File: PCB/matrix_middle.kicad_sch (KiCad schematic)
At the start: 62 parts, among them J10 Conn_02x04_Top_Bottom, J11 Conn_01x04, J12 Conn_02x04_Top_Bottom, J13 Conn_01x04, J14 Conn_02x04_Top_Bottom, J15 Conn_02x02_Top_Bottom, J17 Conn_02x02_Top_Bottom, J19 Conn_02x02_Top_Bottom, J20 Conn_02x02_Top_Bottom, J25 Conn_01x04, J27 Conn_01x04, J9 Conn_02x04_Top_Bottom

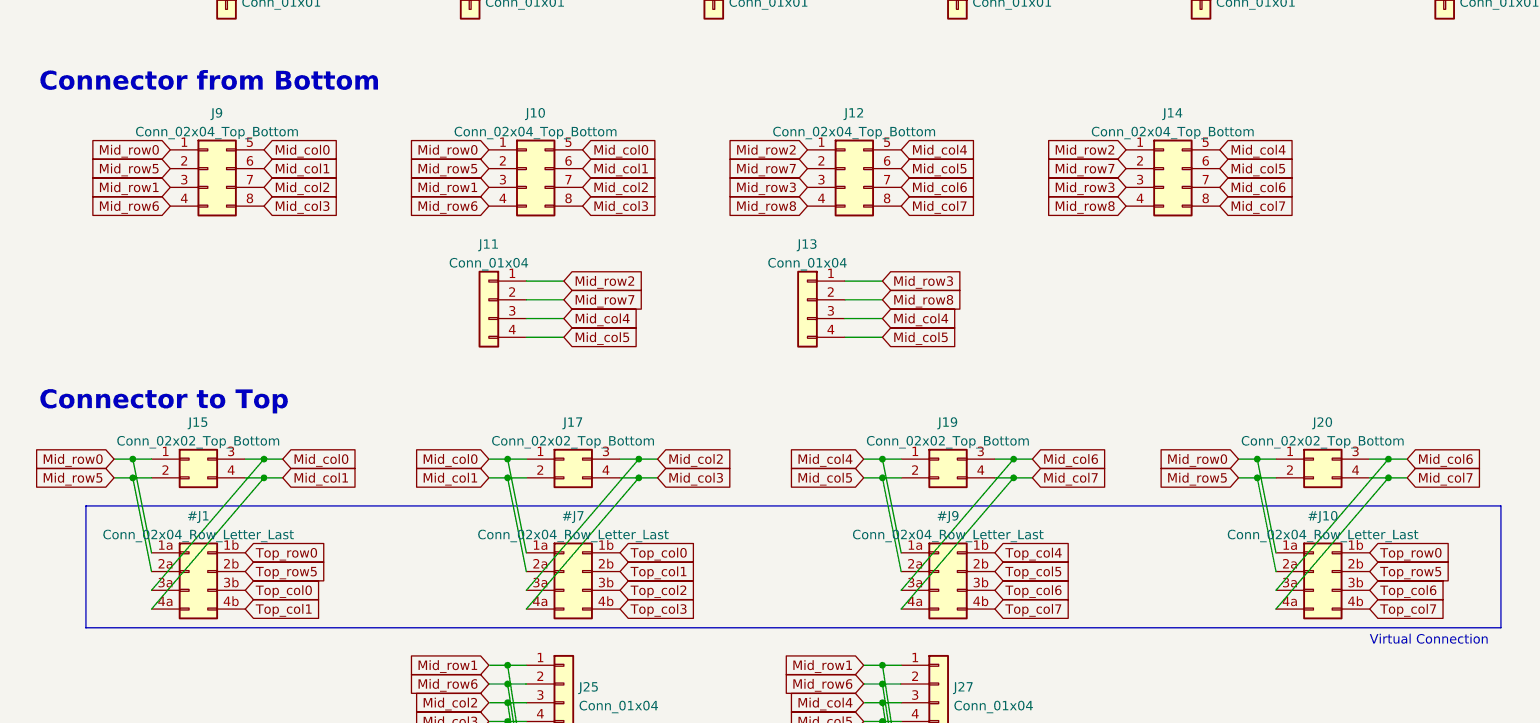
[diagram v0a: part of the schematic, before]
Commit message: ピンヘッダのピン順を変更。フットプリント割り当て。
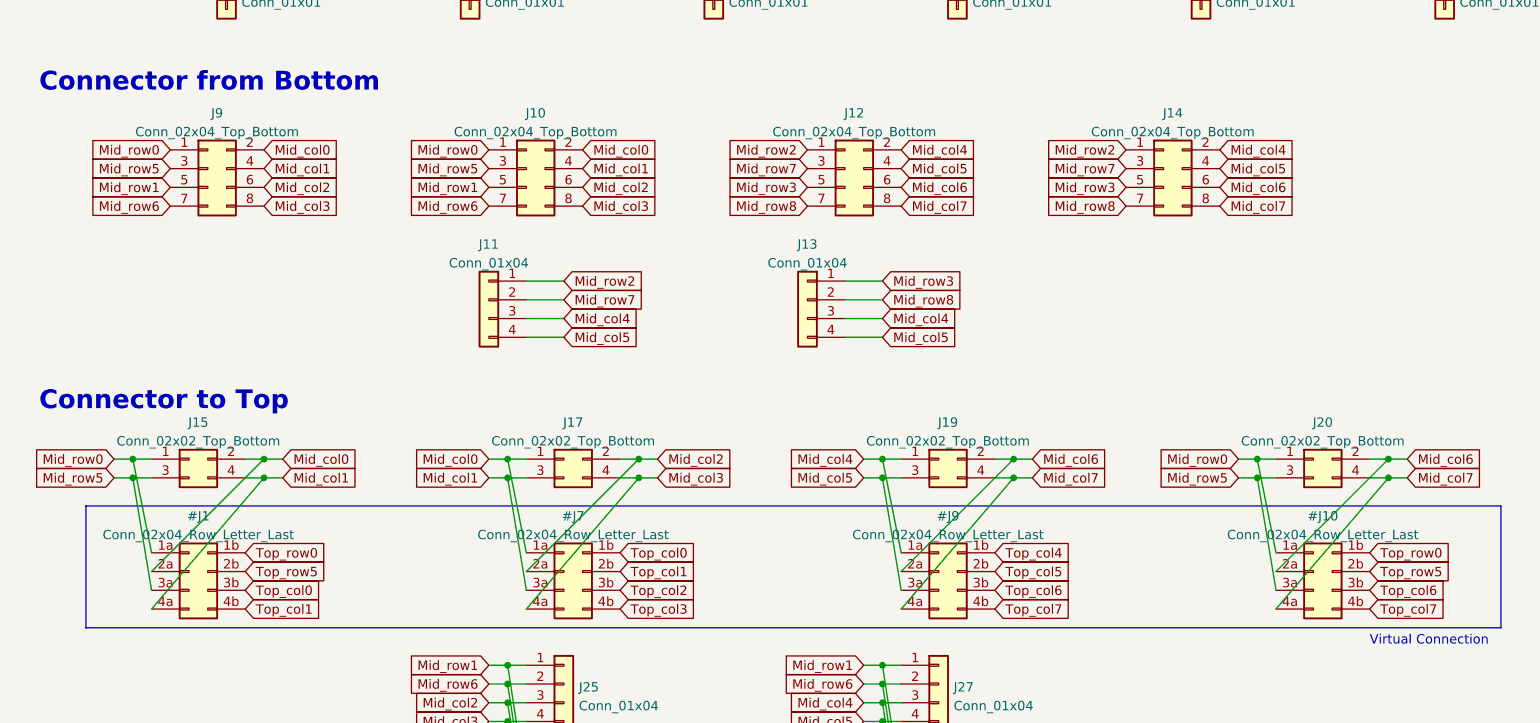
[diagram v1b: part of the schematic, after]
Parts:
- EXT_C10, EXT_C11, EXT_C12, EXT_C13, EXT_C14, EXT_C15, EXT_C8, EXT_C9, EXT_R10, EXT_R11, EXT_R12, EXT_R13, EXT_R14, EXT_R15, EXT_R16, EXT_R17: footprint TestPoint:TestPoint_THTPad_D1.5mm_Drill0.7mm -> TestPoint:TestPoint_THTPad_D2.0mm_Drill1.0mm
- J10, J12, J14, J9: footprint (none) -> Connector_PinHeader_2.54mm:PinHeader_2x04_P2.54mm_Vertical; symbol Connector_Generic:Conn_02x04_Top_Bottom -> Connector_Generic:Conn_02x04_Odd_Even
- J11, J13, J25, J27: footprint (none) -> Connector_PinHeader_2.54mm:PinHeader_1x04_P2.54mm_Vertical
- J15, J17, J19, J20: footprint (none) -> Connector_PinHeader_2.54mm:PinHeader_2x02_P2.54mm_Vertical; symbol Connector_Generic:Conn_02x02_Top_Bottom -> Connector_Generic:Conn_02x02_Odd_Even
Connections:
- net Mid_col0: now also #J1.2a (Pin_2a), J10.2 (Pin_2), J15.2 (Pin_2), J9.2 (Pin_2); no longer #J1.3a (Pin_3a), J10.5 (Pin_5), J15.3 (Pin_3), J9.5 (Pin_5)
- net Mid_col1: now also #J7.3a (Pin_3a), J10.4 (Pin_4), J17.3 (Pin_3), J9.4 (Pin_4); no longer #J7.2a (Pin_2a), J10.6 (Pin_6), J17.2 (Pin_2), J9.6 (Pin_6)
- net Mid_col2: now also #J7.2a (Pin_2a), J10.6 (Pin_6), J17.2 (Pin_2), J9.6 (Pin_6); no longer #J7.3a (Pin_3a), J10.7 (Pin_7), J17.3 (Pin_3), J9.7 (Pin_7)
- net Mid_col4: now also J12.2 (Pin_2), J14.2 (Pin_2); no longer J12.5 (Pin_5), J14.5 (Pin_5)
- net Mid_col5: now also #J9.3a (Pin_3a), J12.4 (Pin_4), J14.4 (Pin_4), J19.3 (Pin_3); no longer #J9.2a (Pin_2a), J12.6 (Pin_6), J14.6 (Pin_6), J19.2 (Pin_2)
- net Mid_col6: now also #J10.2a (Pin_2a), #J9.2a (Pin_2a), J12.6 (Pin_6), J14.6 (Pin_6), J19.2 (Pin_2), J20.2 (Pin_2); no longer #J10.3a (Pin_3a), #J9.3a (Pin_3a), J12.7 (Pin_7), J14.7 (Pin_7), J19.3 (Pin_3), J20.3 (Pin_3)
- net Mid_row1: now also J10.5 (Pin_5), J9.5 (Pin_5); no longer J10.3 (Pin_3), J9.3 (Pin_3)
- net Mid_row3: now also J12.5 (Pin_5), J14.5 (Pin_5); no longer J12.3 (Pin_3), J14.3 (Pin_3)
- net Mid_row5: now also #J1.3a (Pin_3a), #J10.3a (Pin_3a), J10.3 (Pin_3), J15.3 (Pin_3), J20.3 (Pin_3), J9.3 (Pin_3); no longer #J1.2a (Pin_2a), #J10.2a (Pin_2a), J10.2 (Pin_2), J15.2 (Pin_2), J20.2 (Pin_2), J9.2 (Pin_2)
- net Mid_row6: now also J10.7 (Pin_7), J9.7 (Pin_7); no longer J10.4 (Pin_4), J9.4 (Pin_4)
- net Mid_row7: now also J12.3 (Pin_3), J14.3 (Pin_3); no longer J12.2 (Pin_2), J14.2 (Pin_2)
- net Mid_row8: now also J12.7 (Pin_7), J14.7 (Pin_7); no longer J12.4 (Pin_4), J14.4 (Pin_4)

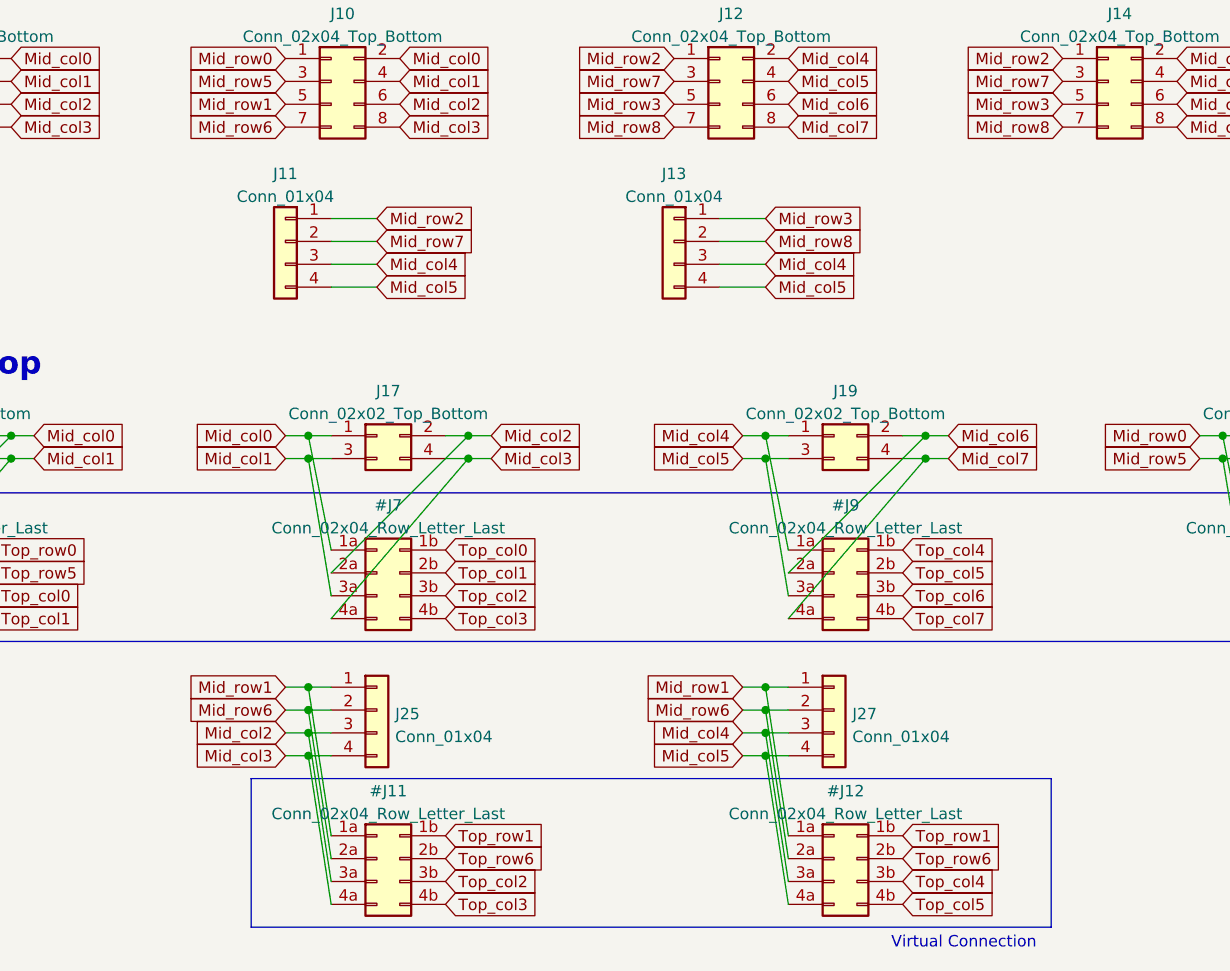
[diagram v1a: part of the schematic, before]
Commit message: 子基板仮配置。コネクタ形状、位置を変更。
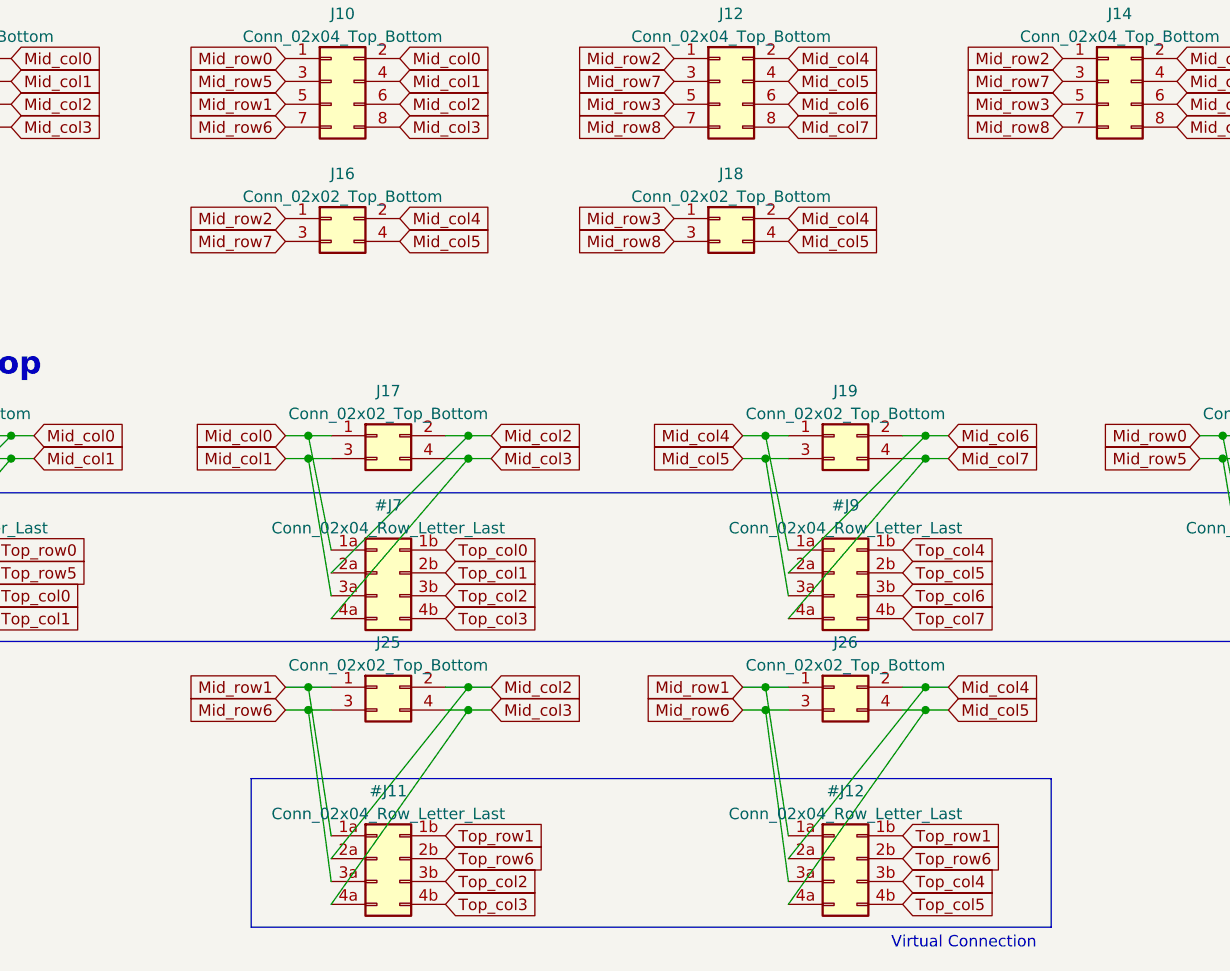
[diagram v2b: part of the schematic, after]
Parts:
- removed J11, J13, J25, J27: Conn_01x04, Connector_PinHeader_2.54mm:PinHeader_1x04_P2.54mm_Vertical, symbol Connector_Generic:Conn_01x04
- added J16, J18, J25, J26: Conn_02x02_Top_Bottom, Connector_PinHeader_2.54mm:PinHeader_2x02_P2.54mm_Vertical, symbol Connector_Generic:Conn_02x02_Odd_Even
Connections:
- net Mid_col2: now also #J11.2a (Pin_2a), J25.2 (Pin_2); no longer #J11.3a (Pin_3a)
- net Mid_col3: now also J25.4 (Pin_4)
- net Mid_col4: now also #J12.2a (Pin_2a), J16.2 (Pin_2), J18.2 (Pin_2), J26.2 (Pin_2); no longer #J12.3a (Pin_3a)
- net Mid_col5: now also J16.4 (Pin_4), J18.4 (Pin_4), J26.4 (Pin_4)
- net Mid_row1: now also J25.1 (Pin_1), J26.1 (Pin_1)
- net Mid_row2: now also J16.1 (Pin_1)
- net Mid_row3: now also J18.1 (Pin_1)
- net Mid_row6: now also #J11.3a (Pin_3a), #J12.3a (Pin_3a), J25.3 (Pin_3), J26.3 (Pin_3); no longer #J11.2a (Pin_2a), #J12.2a (Pin_2a)
- net Mid_row7: now also J16.3 (Pin_3)
- net Mid_row8: now also J18.3 (Pin_3)

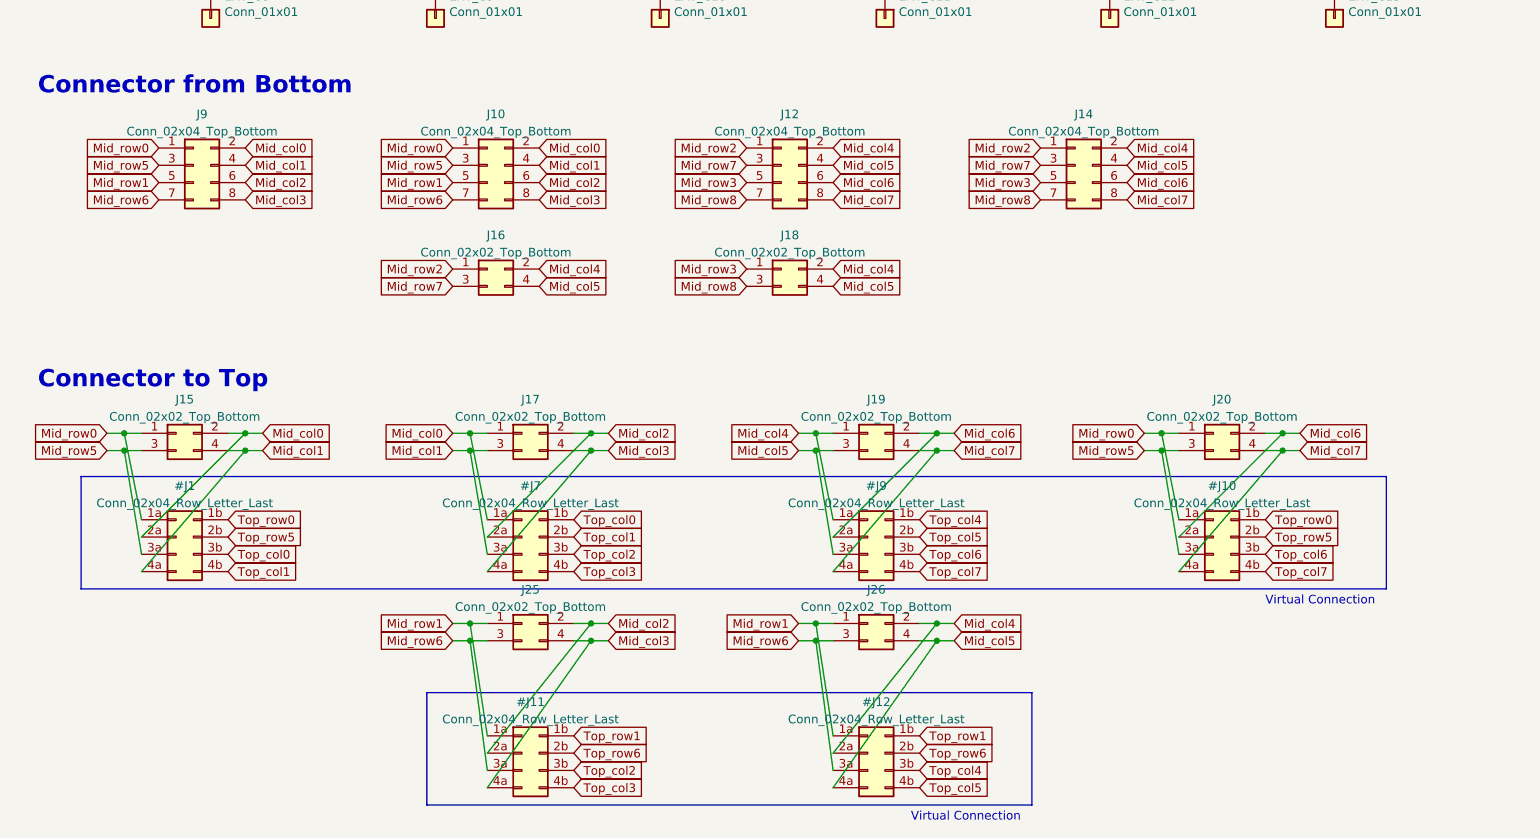
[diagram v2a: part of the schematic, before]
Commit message: 外形、ネジ穴調整
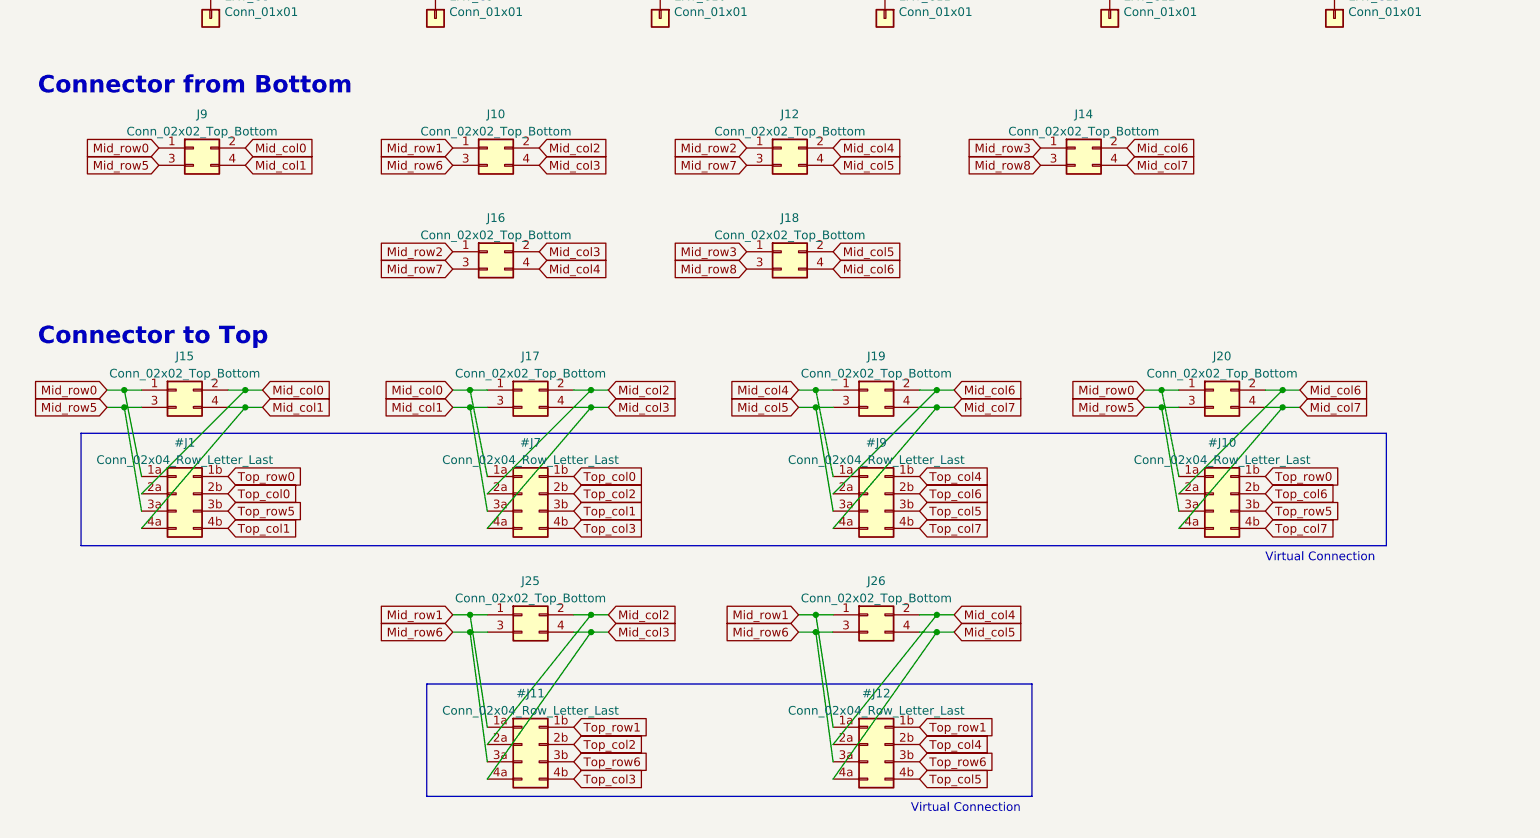
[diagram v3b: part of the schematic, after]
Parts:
- removed J10, J12, J14, J9: Conn_02x04_Top_Bottom, Connector_PinHeader_2.54mm:PinHeader_2x04_P2.54mm_Vertical, symbol Connector_Generic:Conn_02x04_Odd_Even
- added J10, J12, J14, J9: Conn_02x02_Top_Bottom, Connector_PinHeader_2.54mm:PinHeader_2x02_P2.54mm_Vertical, symbol Connector_Generic:Conn_02x02_Odd_Even
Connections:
- net Mid_col0: now also J9.2 (Pin_2)
- net Mid_col1: now also J9.4 (Pin_4)
- net Mid_col2: now also J10.2 (Pin_2)
- net Mid_col3: now also J16.2 (Pin_2), J10.4 (Pin_4)
- net Mid_col4: now also J16.4 (Pin_4), J12.2 (Pin_2); no longer J16.2 (Pin_2), J18.2 (Pin_2)
- net Mid_col5: now also J18.2 (Pin_2), J12.4 (Pin_4); no longer J16.4 (Pin_4), J18.4 (Pin_4)
- net Mid_col6: now also J18.4 (Pin_4), J14.2 (Pin_2)
- net Mid_col7: now also J14.4 (Pin_4)
- net Mid_row0: now also J9.1 (Pin_1)
- net Mid_row1: now also J10.1 (Pin_1)
- net Mid_row2: now also J12.1 (Pin_1)
- net Mid_row3: now also J14.1 (Pin_1)
- net Mid_row5: now also J9.3 (Pin_3)
- net Mid_row6: now also J10.3 (Pin_3)
- net Mid_row7: now also J12.3 (Pin_3)
- net Mid_row8: now also J14.3 (Pin_3)
- net Top_col0: now also #J1.2b (Pin_2b); no longer #J1.3b (Pin_3b)
- net Top_col1: now also #J7.3b (Pin_3b); no longer #J7.2b (Pin_2b)
- net Top_col2: now also #J11.2b (Pin_2b), #J7.2b (Pin_2b); no longer #J11.3b (Pin_3b), #J7.3b (Pin_3b)
- net Top_col4: now also #J12.2b (Pin_2b); no longer #J12.3b (Pin_3b)
- net Top_col5: now also #J9.3b (Pin_3b); no longer #J9.2b (Pin_2b)
- net Top_col6: now also #J10.2b (Pin_2b), #J9.2b (Pin_2b); no longer #J10.3b (Pin_3b), #J9.3b (Pin_3b)
- net Top_row5: now also #J1.3b (Pin_3b), #J10.3b (Pin_3b); no longer #J1.2b (Pin_2b), #J10.2b (Pin_2b)
- net Top_row6: now also #J11.3b (Pin_3b), #J12.3b (Pin_3b); no longer #J11.2b (Pin_2b), #J12.2b (Pin_2b)
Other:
- moved on the sheet: J15, J16, J17, J18, J19, J20, J25, J26
